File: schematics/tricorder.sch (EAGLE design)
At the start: 73 parts, among them IC1 EADOGM128, Q1 MOSFET-NCHANNELBSS138, U1 V_REG_LDOSMD, U2 CY8C5XXX, U3 M05X2-0.05-SMD, U7 MICROUSB, Y1 XRCGB_XTAL

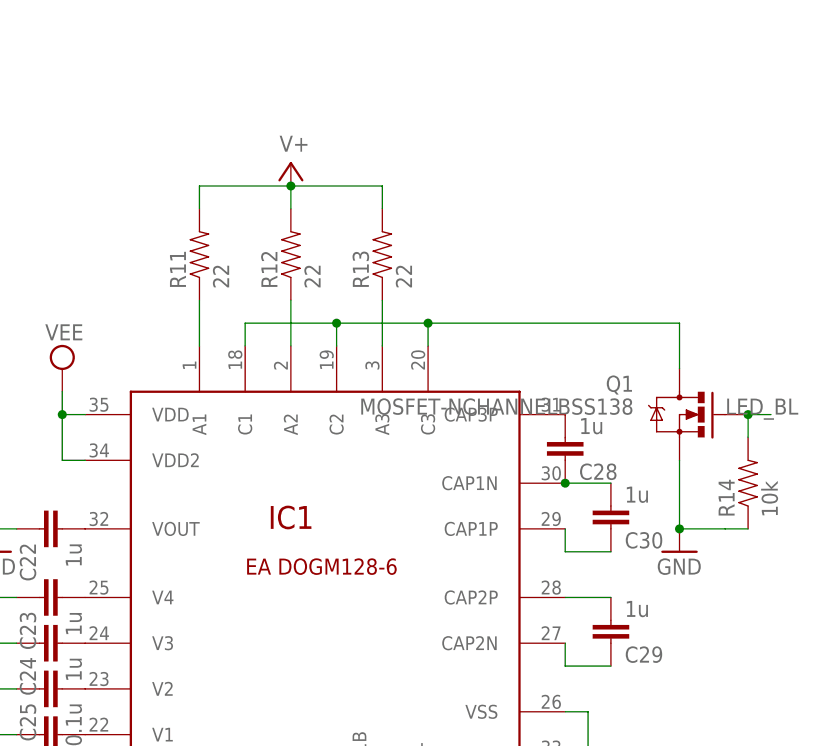
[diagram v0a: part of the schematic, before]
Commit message: Design and layout modifications: onboard BNC, dedicated backlight controller
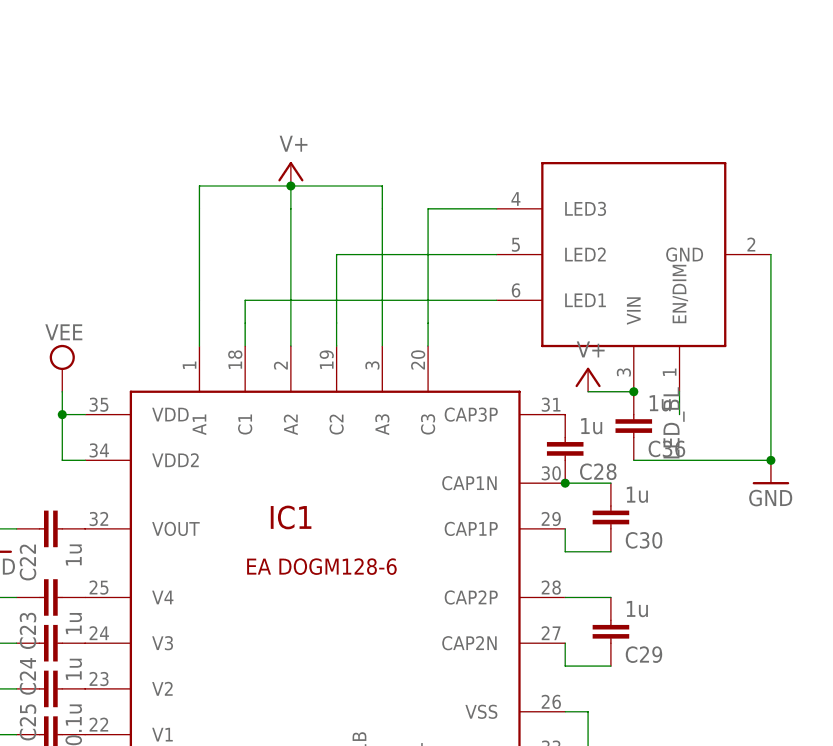
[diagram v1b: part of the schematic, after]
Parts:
- removed Q1: MOSFET-NCHANNELBSS138, SparkFun-DiscreteSemi:MOSFET-NCHANNELBSS138
- removed R11, R12, R13: 22, SparkFun-Passives:RESISTOR0603-RES
- removed R14: 10k, SparkFun-Passives:RESISTOR0603-RES
- added C36: 1u, resistor:C-EUC0603K
- added U$16: CAT4003B, nickparts:CAT4003B
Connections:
- removed net N$24: IC1.C1, IC1.C2, IC1.C3, Q1.D
- net GND: now also C36.1, U$16.GND; no longer Q1.S, R14.1
- net LED_BL: now also U$16.EN/DIM; no longer Q1.G, R14.2
- net N$22: now also IC1.C1, U$16.LED1; no longer IC1.A1, R11.1
- net N$23: now also IC1.C2, U$16.LED2; no longer IC1.A2, R12.1
- net N$25: now also IC1.C3, U$16.LED3; no longer IC1.A3, R13.1
- net V+: now also C36.2, IC1.A1, IC1.A2, IC1.A3, U$16.VIN; no longer R11.2, R12.2, R13.2
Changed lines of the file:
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@@
 <part name="C29" library="resistor" deviceset="C-EU" device="C0603K" value="1u"/>
 <part name="C30" library="resistor" deviceset="C-EU" device="C0603K" value="1u"/>
-<part name="Q1" library="SparkFun-DiscreteSemi" deviceset="MOSFET-NCHANNEL" device="BSS138"/>
-<part name="R11" library="SparkFun-Passives" deviceset="RESISTOR" device="0603-RES" value="22"/>
-<part name="R12" library="SparkFun-Passives" deviceset="RESISTOR" device="0603-RES" value="22"/>
-<part name="R13" library="SparkFun-Passives" deviceset="RESISTOR" device="0603-RES" value="22"/>
 <part name="GND1" library="supply1" deviceset="GND" device=""/>
 <part name="SUPPLY21" library="supply2" deviceset="V+" device=""/>
@@
 <part name="GND13" library="supply1" deviceset="GND" device=""/>
 <part name="U$15" library="ea-dogm" deviceset="EAWF100-04S" device=""/>
-<part name="R14" library="SparkFun-Passives" deviceset="RESISTOR" device="0603-RES" value="10k"/>
 <part name="U$4" library="nickparts" deviceset="BNC" device=""/>
 <part name="U$11" library="nickparts" deviceset="BNC" device=""/>
@@
 <part name="C35" library="resistor" deviceset="C-EU" device="C0603K" value="1u"/>
 <part name="AGND8" library="supply1" deviceset="AGND" device=""/>
+<part name="U$16" library="nickparts" deviceset="CAT4003B" device=""/>
+<part name="SUPPLY16" library="supply2" deviceset="V+" device=""/>
+<part name="C36" library="resistor" deviceset="C-EU" device="C0603K" value="1u"/>
 </parts>
 <sheets>
@@
 <instance part="C29" gate="G$1" x="363.22" y="78.74" rot="MR180"/>
 <instance part="C30" gate="G$1" x="363.22" y="91.44" rot="MR180"/>
-<instance part="Q1" gate="G$1" x="370.84" y="104.14" rot="MR0"/>
-<instance part="R11" gate="G$1" x="317.5" y="121.92" rot="R90"/>
-<instance part="R12" gate="G$1" x="327.66" y="121.92" rot="R90"/>
-<instance part="R13" gate="G$1" x="337.82" y="121.92" rot="R90"/>
 <instance part="GND1" gate="1" x="246.38" y="116.84"/>
 <instance part="SUPPLY21" gate="1" x="15.24" y="137.16"/>
@@
 <instance part="GND6" gate="1" x="294.64" y="88.9"/>
 <instance part="GND7" gate="1" x="360.68" y="60.96"/>
-<instance part="GND10" gate="1" x="370.84" y="88.9"/>
+<instance part="GND10" gate="1" x="381" y="96.52"/>
 <instance part="C31" gate="G$1" x="144.78" y="241.3"/>
 <instance part="C32" gate="G$1" x="177.8" y="238.76"/>
@@
 <instance part="GND13" gate="1" x="167.64" y="55.88"/>
 <instance part="U$15" gate="G$1" x="160.02" y="33.02"/>
-<instance part="R14" gate="G$1" x="378.46" y="96.52" rot="R90"/>
 <instance part="U$4" gate="G$1" x="55.88" y="55.88" rot="R90"/>
 <instance part="U$11" gate="G$1" x="55.88" y="12.7" rot="R90"/>
@@
 <instance part="C35" gate="G$1" x="119.38" y="231.14"/>
 <instance part="AGND8" gate="VR1" x="119.38" y="223.52"/>
+<instance part="U$16" gate="G$1" x="363.22" y="121.92" rot="R90"/>
+<instance part="SUPPLY16" gate="1" x="360.68" y="109.22"/>
+<instance part="C36" gate="G$1" x="365.76" y="101.6" rot="MR180"/>
 </instances>
 <busses>
@@
 </segment>
 <segment>
-<pinref part="Q1" gate="G$1" pin="S"/>
-<pinref part="GND10" gate="1" pin="GND"/>
-<wire x1="370.84" y1="91.44" x2="370.84" y2="99.06" width="0.1524" layer="91"/>
-<wire x1="370.84" y1="91.44" x2="375.92" y2="91.44" width="0.1524" layer="91"/>
-<junction x="370.84" y="91.44"/>
-<pinref part="R14" gate="G$1" pin="1"/>
-<wire x1="378.46" y1="91.44" x2="375.92" y2="91.44" width="0.1524" layer="91"/>
-</segment>
-<segment>
 <pinref part="U$7" gate="G$1" pin="P$1"/>
 <wire x1="20.32" y1="241.3" x2="20.32" y2="238.76" width="0.1524" layer="91"/>
@@
 <pinref part="GND13" gate="1" pin="GND"/>
 </segment>
+<segment>
+<pinref part="U$16" gate="G$1" pin="GND"/>
+<pinref part="GND10" gate="1" pin="GND"/>
+<wire x1="381" y1="99.06" x2="381" y2="121.92" width="0.1524" layer="91"/>
+<pinref part="C36" gate="G$1" pin="1"/>
+<wire x1="365.76" y1="99.06" x2="381" y2="99.06" width="0.1524" layer="91"/>
+<junction x="381" y="99.06"/>
+</segment>
 </net>
 <net name="SWDIO" class="0">
@@
 </segment>
 <segment>
-<pinref part="R13" gate="G$1" pin="2"/>
 <wire x1="337.82" y1="127" x2="337.82" y2="129.54" width="0.1524" layer="91"/>
 <wire x1="337.82" y1="129.54" x2="327.66" y2="129.54" width="0.1524" layer="91"/>
-<pinref part="R11" gate="G$1" pin="2"/>
 <wire x1="327.66" y1="129.54" x2="317.5" y2="129.54" width="0.1524" layer="91"/>
 <wire x1="317.5" y1="127" x2="317.5" y2="129.54" width="0.1524" layer="91"/>
-<pinref part="R12" gate="G$1" pin="2"/>
 <wire x1="327.66" y1="127" x2="327.66" y2="129.54" width="0.1524" layer="91"/>
 <junction x="327.66" y="129.54"/>
 <pinref part="SUPPLY12" gate="1" pin="V+"/>
+<pinref part="IC1" gate="G$1" pin="A1"/>
+<wire x1="317.5" y1="111.76" x2="317.5" y2="116.84" width="0.1524" layer="91"/>
+<wire x1="317.5" y1="116.84" x2="317.5" y2="127" width="0.1524" layer="91"/>
+<pinref part="IC1" gate="G$1" pin="A2"/>
+<wire x1="327.66" y1="111.76" x2="327.66" y2="116.84" width="0.1524" layer="91"/>
+<wire x1="327.66" y1="127" x2="327.66" y2="116.84" width="0.1524" layer="91"/>
+<pinref part="IC1" gate="G$1" pin="A3"/>
+<wire x1="337.82" y1="111.76" x2="337.82" y2="116.84" width="0.1524" layer="91"/>
+<wire x1="337.82" y1="127" x2="337.82" y2="116.84" width="0.1524" layer="91"/>
+</segment>
+<segment>
+<pinref part="SUPPLY16" gate="1" pin="V+"/>
+<pinref part="U$16" gate="G$1" pin="VIN"/>
+<wire x1="360.68" y1="106.68" x2="365.76" y2="106.68" width="0.1524" layer="91"/>
+<pinref part="C36" gate="G$1" pin="2"/>
+<junction x="365.76" y="106.68"/>
 </segment>
 </net>
@@
 </segment>
 </net>
-<net name="N$24" class="0">
-<segment>
-<pinref part="IC1" gate="G$1" pin="C3"/>
-<wire x1="342.9" y1="111.76" x2="342.9" y2="114.3" width="0.1524" layer="91"/>
-<pinref part="Q1" gate="G$1" pin="D"/>
-<wire x1="342.9" y1="114.3" x2="370.84" y2="114.3" width="0.1524" layer="91"/>
-<wire x1="370.84" y1="114.3" x2="370.84" y2="109.22" width="0.1524" layer="91"/>
-<pinref part="IC1" gate="G$1" pin="C2"/>
-<wire x1="342.9" y1="114.3" x2="332.74" y2="114.3" width="0.1524" layer="91"/>
-<wire x1="332.74" y1="114.3" x2="332.74" y2="111.76" width="0.1524" layer="91"/>
-<junction x="342.9" y="114.3"/>
-<pinref part="IC1" gate="G$1" pin="C1"/>
-<wire x1="332.74" y1="114.3" x2="322.58" y2="114.3" width="0.1524" layer="91"/>
-<wire x1="322.58" y1="114.3" x2="322.58" y2="111.76" width="0.1524" layer="91"/>
-<junction x="332.74" y="114.3"/>
-</segment>
-</net>
-<net name="N$22" class="0">
-<segment>
-<pinref part="IC1" gate="G$1" pin="A1"/>
-<pinref part="R11" gate="G$1" pin="1"/>
-<wire x1="317.5" y1="111.76" x2="317.5" y2="116.84" width="0.1524" layer="91"/>
-</segment>
-</net>
-<net name="N$23" class="0">
-<segment>
-<pinref part="IC1" gate="G$1" pin="A2"/>
-<pinref part="R12" gate="G$1" pin="1"/>
-<wire x1="327.66" y1="111.76" x2="327.66" y2="116.84" width="0.1524" layer="91"/>
-</segment>
-</net>
-<net name="N$25" class="0">
-<segment>
-<pinref part="IC1" gate="G$1" pin="A3"/>
-<pinref part="R13" gate="G$1" pin="1"/>
-<wire x1="337.82" y1="111.76" x2="337.82" y2="116.84" width="0.1524" layer="91"/>
-</segment>
-</net>
 <net name="LED_BL" class="0">
-<segment>
-<pinref part="Q1" gate="G$1" pin="G"/>
-<wire x1="378.46" y1="104.14" x2="381" y2="104.14" width="0.1524" layer="91"/>
-<label x="375.92" y="104.14" size="1.778" layer="95"/>
-<pinref part="R14" gate="G$1" pin="2"/>
-<wire x1="378.46" y1="101.6" x2="378.46" y2="104.14" width="0.1524" layer="91"/>
-<junction x="378.46" y="104.14"/>
-</segment>
 <segment>
 <pinref part="U2" gate="G$1" pin="P1_6"/>
 <wire x1="81.28" y1="114.3" x2="81.28" y2="111.76" width="0.1524" layer="91"/>
 <label x="81.28" y="106.68" size="1.778" layer="95" rot="R90"/>
+</segment>
+<segment>
+<pinref part="U$16" gate="G$1" pin="EN/DIM"/>
+<wire x1="370.84" y1="106.68" x2="370.84" y2="104.14" width="0.1524" layer="91"/>
+<label x="370.84" y="99.06" size="1.778" layer="95" rot="R90"/>
 </segment>
 </net>
@@
 </segment>
 </net>
+<net name="N$22" class="0">
+<segment>
+<pinref part="IC1" gate="G$1" pin="C1"/>
+<wire x1="322.58" y1="114.3" x2="322.58" y2="111.76" width="0.1524" layer="91"/>
+<pinref part="U$16" gate="G$1" pin="LED1"/>
+<wire x1="350.52" y1="116.84" x2="322.58" y2="116.84" width="0.1524" layer="91"/>
+<wire x1="322.58" y1="116.84" x2="322.58" y2="114.3" width="0.1524" layer="91"/>
+</segment>
+</net>
+<net name="N$23" class="0">
+<segment>
+<pinref part="IC1" gate="G$1" pin="C2"/>
+<wire x1="332.74" y1="114.3" x2="332.74" y2="111.76" width="0.1524" layer="91"/>
+<pinref part="U$16" gate="G$1" pin="LED2"/>
+<wire x1="350.52" y1="121.92" x2="332.74" y2="121.92" width="0.1524" layer="91"/>
+<wire x1="332.74" y1="121.92" x2="332.74" y2="114.3" width="0.1524" layer="91"/>
+</segment>
+</net>
+<net name="N$25" class="0">
+<segment>
+<pinref part="IC1" gate="G$1" pin="C3"/>
+<wire x1="342.9" y1="111.76" x2="342.9" y2="114.3" width="0.1524" layer="91"/>
+<pinref part="U$16" gate="G$1" pin="LED3"/>
+<wire x1="350.52" y1="127" x2="342.9" y2="127" width="0.1524" layer="91"/>
+<wire x1="342.9" y1="127" x2="342.9" y2="114.3" width="0.1524" layer="91"/>
+</segment>
+</net>

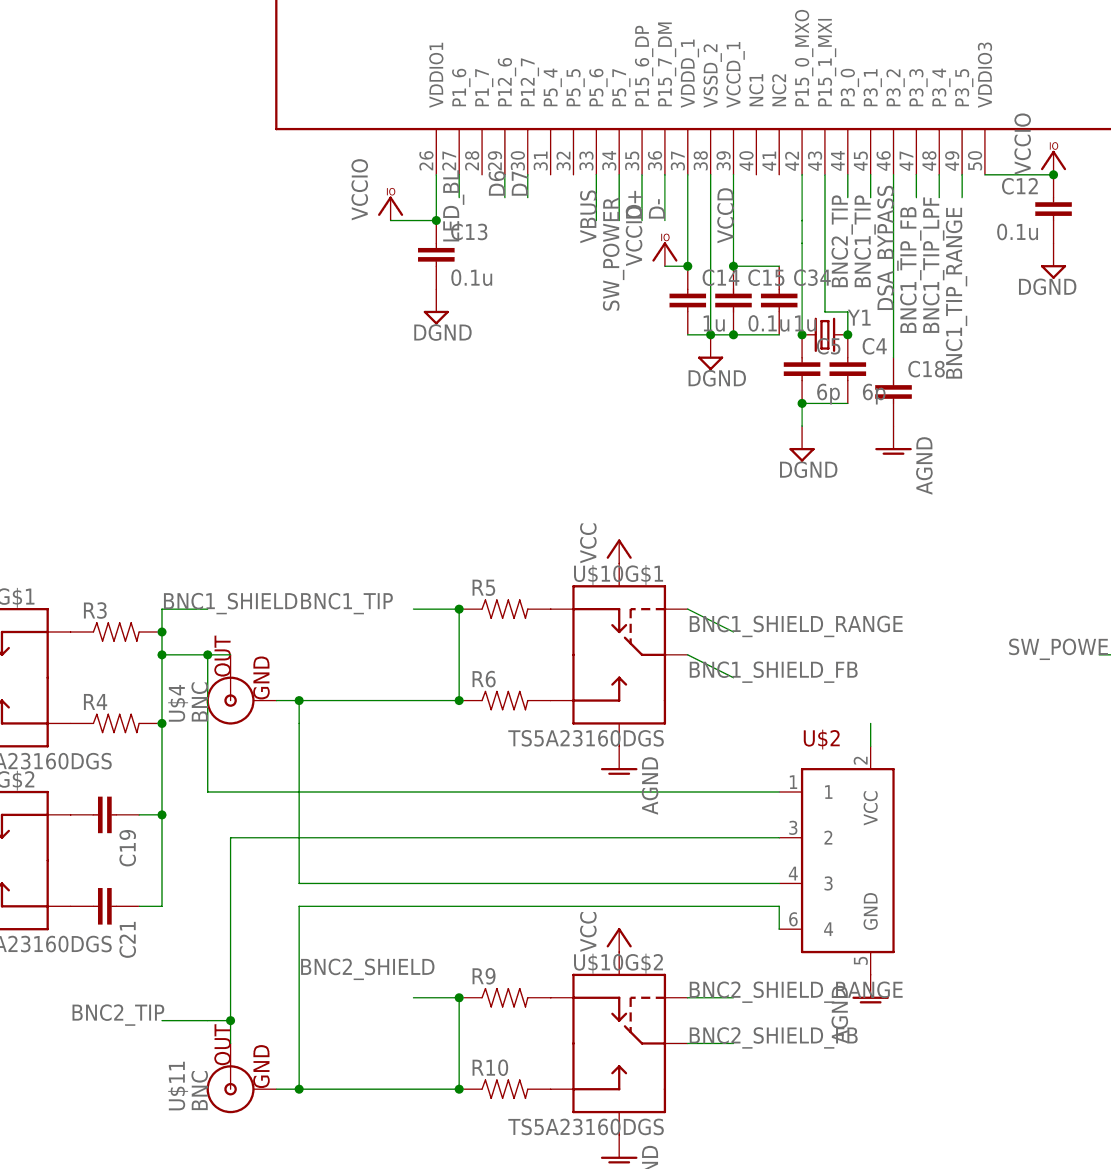
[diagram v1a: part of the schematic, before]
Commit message: Modified tricorder code so it compiles in a basic fashion; TRM and schematic fixes.
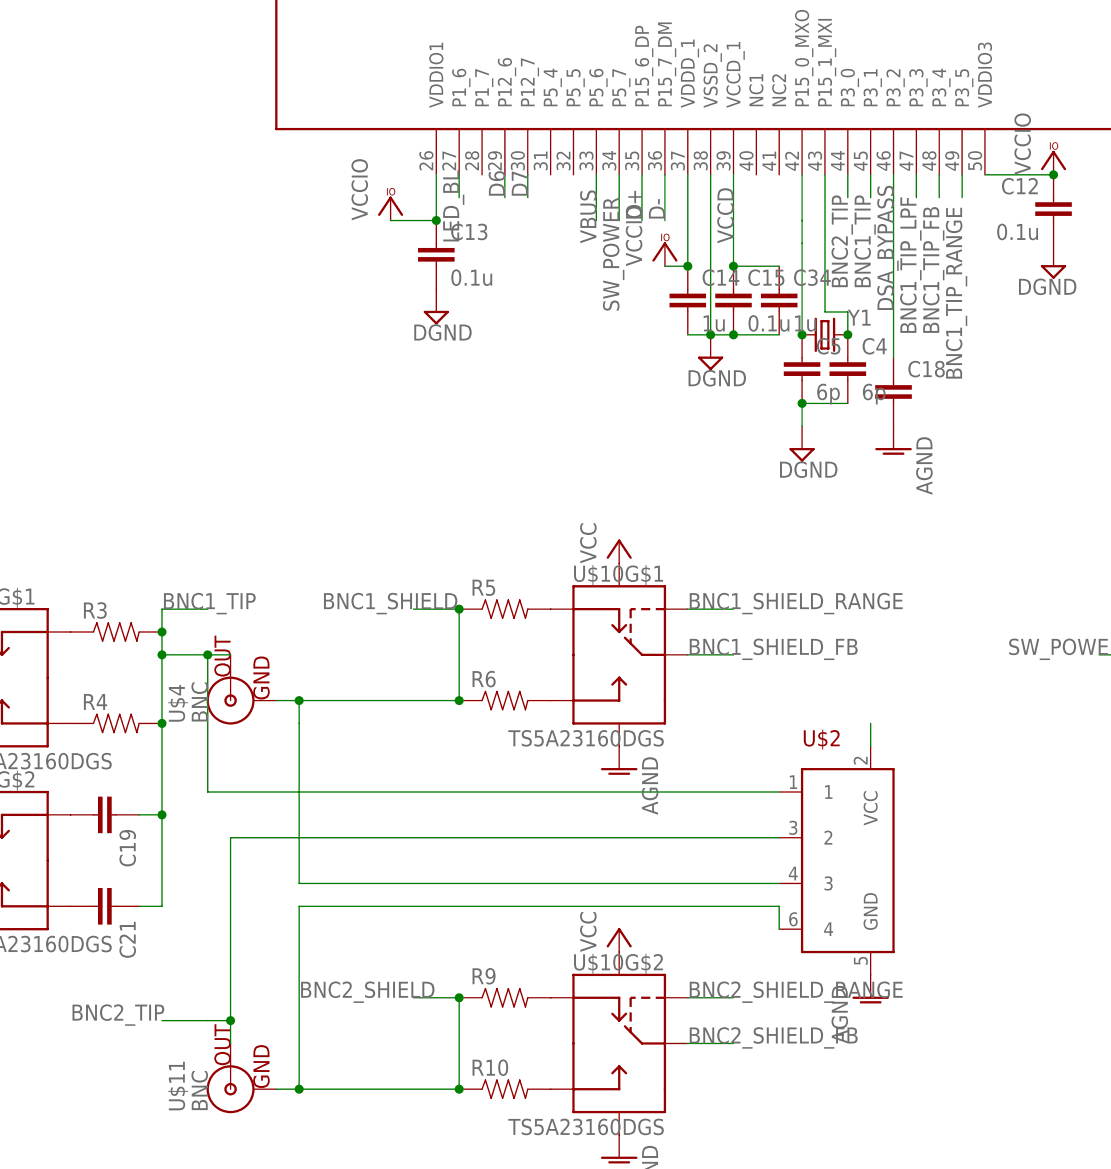
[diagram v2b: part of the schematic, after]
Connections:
- net BNC1_SHIELD: now also R5.1, R6.1, U$2.3, U$4.GND; no longer C19.1, C21.1, R3.2, R4.2, U$2.1, U$4.OUT
- net BNC1_TIP: now also C19.1, C21.1, R3.2, R4.2, U$2.1, U$4.OUT; no longer R5.1, R6.1, U$2.3, U$4.GND
- net BNC1_TIP_FB: now also U2.P3_4; no longer U2.P3_3
- net BNC1_TIP_LPF: now also U2.P3_3; no longer U2.P3_4
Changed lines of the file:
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@@
 </segment>
-<segment>
-<pinref part="R5" gate="G$1" pin="1"/>
-<wire x1="81.28" y1="66.04" x2="76.2" y2="66.04" width="0.1524" layer="91"/>
-<junction x="81.28" y="66.04"/>
-<pinref part="R6" gate="G$1" pin="1"/>
-<wire x1="81.28" y1="55.88" x2="81.28" y2="66.04" width="0.1524" layer="91"/>
-<junction x="81.28" y="55.88"/>
-<wire x1="60.96" y1="55.88" x2="63.5" y2="55.88" width="0.1524" layer="91"/>
-<wire x1="63.5" y1="55.88" x2="81.28" y2="55.88" width="0.1524" layer="91"/>
-<junction x="63.5" y="55.88"/>
-<wire x1="63.5" y1="53.34" x2="63.5" y2="55.88" width="0.1524" layer="91"/>
-<label x="63.5" y="66.04" size="1.778" layer="95"/>
-<pinref part="U$4" gate="G$1" pin="GND"/>
-<pinref part="U$2" gate="G$1" pin="3"/>
-<wire x1="116.84" y1="35.56" x2="63.5" y2="35.56" width="0.1524" layer="91"/>
-<wire x1="63.5" y1="35.56" x2="63.5" y2="53.34" width="0.1524" layer="91"/>
-</segment>
-</net>
-<net name="BNC1_SHIELD" class="0">
 <segment>
 <pinref part="U$2" gate="G$1" pin="1"/>
@@
 <junction x="53.34" y="60.96"/>
 </segment>
+</net>
+<net name="BNC1_SHIELD" class="0">
 <segment>
 <pinref part="U2" gate="G$1" pin="P0_3"/>
@@
 <wire x1="132.08" y1="220.98" x2="132.08" y2="223.52" width="0.1524" layer="91"/>
 <label x="132.08" y="220.98" size="1.778" layer="95" rot="R90"/>
+</segment>
+<segment>
+<pinref part="R5" gate="G$1" pin="1"/>
+<wire x1="81.28" y1="66.04" x2="76.2" y2="66.04" width="0.1524" layer="91"/>
+<junction x="81.28" y="66.04"/>
+<pinref part="R6" gate="G$1" pin="1"/>
+<wire x1="81.28" y1="55.88" x2="81.28" y2="66.04" width="0.1524" layer="91"/>
+<junction x="81.28" y="55.88"/>
+<wire x1="60.96" y1="55.88" x2="63.5" y2="55.88" width="0.1524" layer="91"/>
+<wire x1="63.5" y1="55.88" x2="81.28" y2="55.88" width="0.1524" layer="91"/>
+<junction x="63.5" y="55.88"/>
+<wire x1="63.5" y1="53.34" x2="63.5" y2="55.88" width="0.1524" layer="91"/>
+<label x="66.04" y="66.04" size="1.778" layer="95"/>
+<pinref part="U$4" gate="G$1" pin="GND"/>
+<pinref part="U$2" gate="G$1" pin="3"/>
+<wire x1="116.84" y1="35.56" x2="63.5" y2="35.56" width="0.1524" layer="91"/>
+<wire x1="63.5" y1="35.56" x2="63.5" y2="53.34" width="0.1524" layer="91"/>
 </segment>
 </net>
@@
 <wire x1="81.28" y1="22.86" x2="76.2" y2="22.86" width="0.1524" layer="91"/>
 <junction x="81.28" y="22.86"/>
-<label x="63.5" y="25.4" size="1.778" layer="95"/>
+<label x="63.5" y="22.86" size="1.778" layer="95"/>
 <wire x1="60.96" y1="12.7" x2="63.5" y2="12.7" width="0.1524" layer="91"/>
 <junction x="63.5" y="12.7"/>
@@
 </segment>
 <segment>
-<pinref part="U2" gate="G$1" pin="P3_3"/>
-<wire x1="132.08" y1="114.3" x2="132.08" y2="111.76" width="0.1524" layer="91"/>
-<label x="132.08" y="96.52" size="1.778" layer="95" rot="R90"/>
+<pinref part="U2" gate="G$1" pin="P3_4"/>
+<wire x1="134.62" y1="114.3" x2="134.62" y2="111.76" width="0.1524" layer="91"/>
+<label x="134.62" y="96.52" size="1.778" layer="95" rot="R90"/>
 </segment>
 </net>
 <net name="BNC1_SHIELD_FB" class="0">
 <segment>
-<wire x1="106.68" y1="60.96" x2="111.76" y2="58.42" width="0.1524" layer="91"/>
-<label x="106.68" y="58.42" size="1.778" layer="95"/>
+<wire x1="106.68" y1="60.96" x2="111.76" y2="60.96" width="0.1524" layer="91"/>
+<label x="106.68" y="60.96" size="1.778" layer="95"/>
 <pinref part="U$10" gate="G$1" pin="COM"/>
 </segment>
@@
 <net name="BNC1_SHIELD_RANGE" class="0">
 <segment>
-<wire x1="106.68" y1="66.04" x2="111.76" y2="63.5" width="0.1524" layer="91"/>
-<label x="106.68" y="63.5" size="1.778" layer="95"/>
+<wire x1="106.68" y1="66.04" x2="111.76" y2="66.04" width="0.1524" layer="91"/>
+<label x="106.68" y="66.04" size="1.778" layer="95"/>
 <pinref part="U$10" gate="G$1" pin="IN"/>
 </segment>
@@
 </segment>
 <segment>
-<pinref part="U2" gate="G$1" pin="P3_4"/>
-<wire x1="134.62" y1="114.3" x2="134.62" y2="111.76" width="0.1524" layer="91"/>
-<label x="134.62" y="96.52" size="1.778" layer="95" rot="R90"/>
-</segment>
-</net>
+<pinref part="U2" gate="G$1" pin="P3_3"/>
+<wire x1="132.08" y1="114.3" x2="132.08" y2="111.76" width="0.1524" layer="91"/>
+<label x="132.08" y="96.52" size="1.778" layer="95" rot="R90"/>
+</segment>
+</net>
